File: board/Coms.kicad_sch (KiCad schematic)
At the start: 12 parts, among them J1 XLR3, J2 XLR3, J8 USB_C_Receptacle_USB2.0, U2 MAX485E

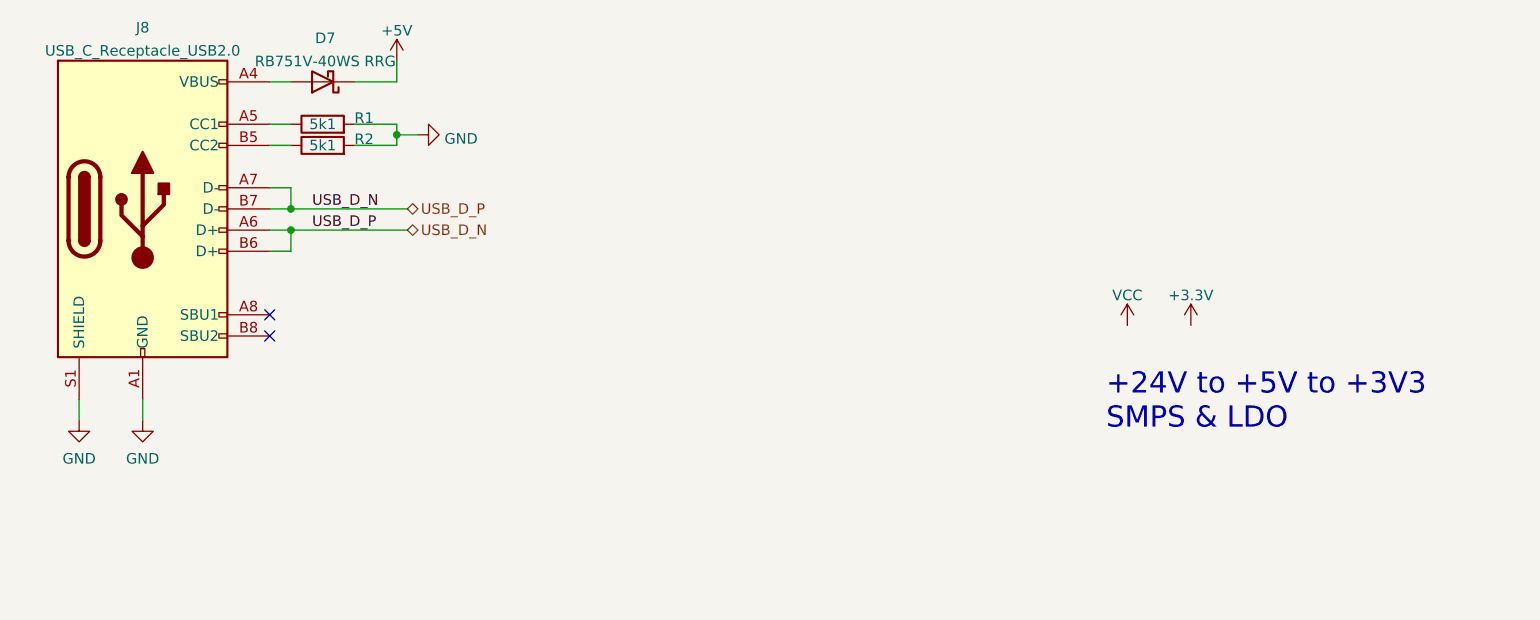
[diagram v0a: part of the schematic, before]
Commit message: doing some cost reduction
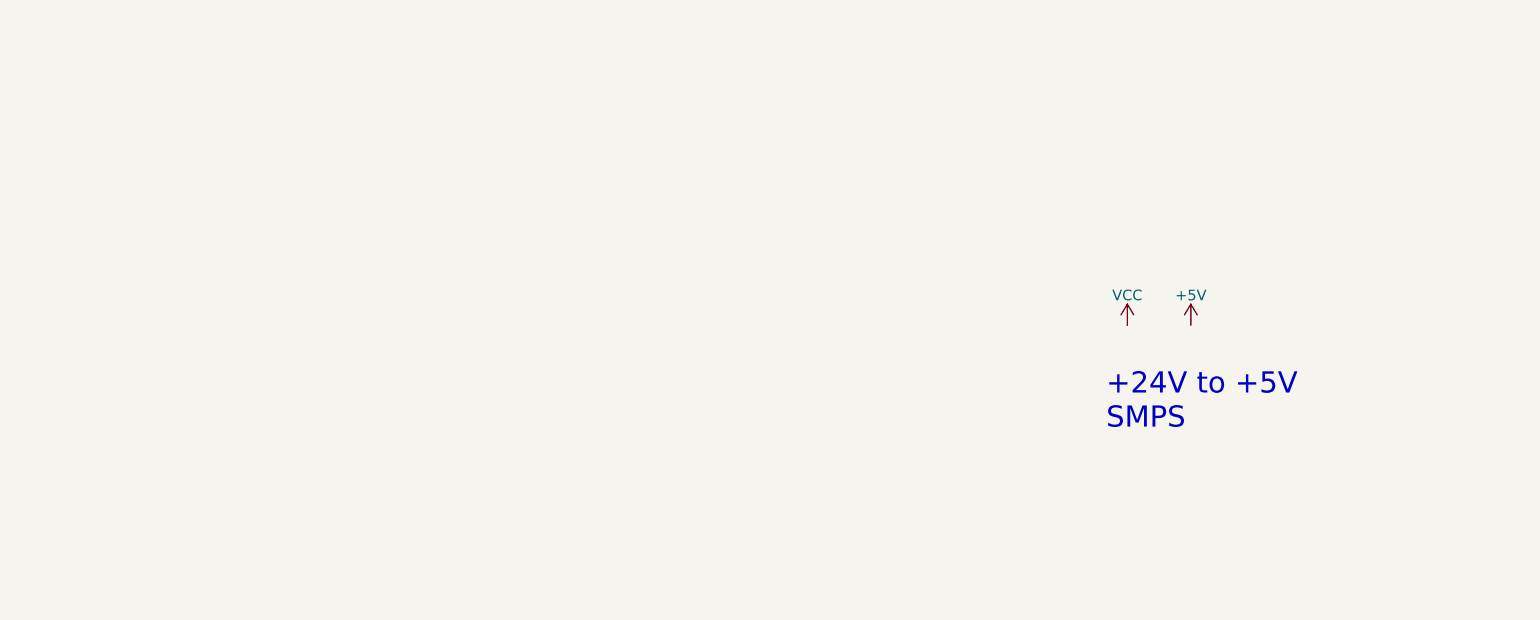
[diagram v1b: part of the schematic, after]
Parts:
- removed D7: RB751V-40WS RRG, Diode_SMD:D_SOD-523, symbol Device:D_Schottky
- removed J8: USB_C_Receptacle_USB2.0, Connector_USB:USB_C_Receptacle_HRO_TYPE-C-31-M-12, symbol Connector:USB_C_Receptacle_USB2.0
- removed R1, R2: 5k1, Resistor_SMD:R_0402_1005Metric, symbol Device:R
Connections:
- no-connect marks 2 -> 0
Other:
- note added: "+24V to +5V SMPS"
- note removed: "+24V to +5V to +3V3 SMPS & LDO"
